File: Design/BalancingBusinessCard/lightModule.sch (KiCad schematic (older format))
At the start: 0 parts

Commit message: Made a part
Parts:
- added D? (x9): LED, symbol Device:LED
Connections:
- new net GND: D?.1 (K), D?.1 (K), D?.1 (K), D?.1 (K), D?.1 (K), D?.1 (K), D?.1 (K), D?.1 (K), D?.1 (K)
- new net LED_0: D?.2 (A)
- new net LED_1: D?.2 (A)
- new net LED_2: D?.2 (A)
- new net LED_3: D?.2 (A)
- new net LED_4: D?.2 (A)
- new net LED_5: D?.2 (A)
- new net LED_6: D?.2 (A)
- new net LED_7: D?.2 (A)
- new net LED_8: D?.2 (A)

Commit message: Assigned numbers
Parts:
- gave numbers to parts that had none: 9
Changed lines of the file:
@@
 $EndDescr
 $Comp
-L Device:LED D?
+L Device:LED D302
 U 1 1 5BCBC85A
 P 3900 2800
-F 0 "D?" V 3938 2683 50  0000 R CNN
+F 0 "D302" V 3938 2683 50  0000 R CNN
 F 1 "LED" V 3847 2683 50  0000 R CNN
 F 2 "" H 3900 2800 50  0001 C CNN
@@
 LED_1
 $Comp
-L power:GND #PWR?
+L power:GND #PWR0117
 U 1 1 5BCBC9E3
 P 3900 3050
-F 0 "#PWR?" H 3900 2800 50  0001 C CNN
+F 0 "#PWR0117" H 3900 2800 50  0001 C CNN
 F 1 "GND" H 3905 2877 50  0000 C CNN
 F 2 "" H 3900 3050 50  0001 C CNN
@@
 	3900 2950 3900 3050
 $Comp
-L Device:LED D?
+L Device:LED D303
 U 1 1 5BCBCA64
 P 4250 2800
-F 0 "D?" V 4288 2683 50  0000 R CNN
+F 0 "D303" V 4288 2683 50  0000 R CNN
 F 1 "LED" V 4197 2683 50  0000 R CNN
 F 2 "" H 4250 2800 50  0001 C CNN
@@
 LED_2
 $Comp
-L power:GND #PWR?
+L power:GND #PWR0118
 U 1 1 5BCBCA6C
 P 4250 3050
-F 0 "#PWR?" H 4250 2800 50  0001 C CNN
+F 0 "#PWR0118" H 4250 2800 50  0001 C CNN
 F 1 "GND" H 4255 2877 50  0000 C CNN
 F 2 "" H 4250 3050 50  0001 C CNN
@@
 	4250 2950 4250 3050
 $Comp
-L Device:LED D?
+L Device:LED D304
 U 1 1 5BCBCA94
 P 4600 2800
-F 0 "D?" V 4638 2683 50  0000 R CNN
+F 0 "D304" V 4638 2683 50  0000 R CNN
 F 1 "LED" V 4547 2683 50  0000 R CNN
 F 2 "" H 4600 2800 50  0001 C CNN
@@
 LED_3
 $Comp
-L power:GND #PWR?
+L power:GND #PWR0119
 U 1 1 5BCBCA9C
 P 4600 3050
-F 0 "#PWR?" H 4600 2800 50  0001 C CNN
+F 0 "#PWR0119" H 4600 2800 50  0001 C CNN
 F 1 "GND" H 4605 2877 50  0000 C CNN
 F 2 "" H 4600 3050 50  0001 C CNN
@@
 	4600 2950 4600 3050
 $Comp
-L Device:LED D?
+L Device:LED D305
 U 1 1 5BCBCAE0
 P 4950 2800
-F 0 "D?" V 4988 2683 50  0000 R CNN
+F 0 "D305" V 4988 2683 50  0000 R CNN
 F 1 "LED" V 4897 2683 50  0000 R CNN
 F 2 "" H 4950 2800 50  0001 C CNN
@@
 LED_4
 $Comp
-L power:GND #PWR?
+L power:GND #PWR0120
 U 1 1 5BCBCAE8
 P 4950 3050
-F 0 "#PWR?" H 4950 2800 50  0001 C CNN
+F 0 "#PWR0120" H 4950 2800 50  0001 C CNN
 F 1 "GND" H 4955 2877 50  0000 C CNN
 F 2 "" H 4950 3050 50  0001 C CNN
@@
 	4950 2950 4950 3050
 $Comp
-L Device:LED D?
+L Device:LED D306
 U 1 1 5BCBCB54
 P 5300 2800
-F 0 "D?" V 5338 2683 50  0000 R CNN
+F 0 "D306" V 5338 2683 50  0000 R CNN
 F 1 "LED" V 5247 2683 50  0000 R CNN
 F 2 "" H 5300 2800 50  0001 C CNN
@@
 LED_5
 $Comp
-L power:GND #PWR?
+L power:GND #PWR0121
 U 1 1 5BCBCB5C
 P 5300 3050
-F 0 "#PWR?" H 5300 2800 50  0001 C CNN
+F 0 "#PWR0121" H 5300 2800 50  0001 C CNN
 F 1 "GND" H 5305 2877 50  0000 C CNN
 F 2 "" H 5300 3050 50  0001 C CNN
@@
 	5300 2950 5300 3050
 $Comp
-L Device:LED D?
+L Device:LED D307
 U 1 1 5BCBCC00
 P 5650 2800
-F 0 "D?" V 5688 2683 50  0000 R CNN
+F 0 "D307" V 5688 2683 50  0000 R CNN
 F 1 "LED" V 5597 2683 50  0000 R CNN
 F 2 "" H 5650 2800 50  0001 C CNN
@@
 LED_6
 $Comp
-L power:GND #PWR?
+L power:GND #PWR0122
 U 1 1 5BCBCC08
 P 5650 3050
-F 0 "#PWR?" H 5650 2800 50  0001 C CNN
+F 0 "#PWR0122" H 5650 2800 50  0001 C CNN
 F 1 "GND" H 5655 2877 50  0000 C CNN
 F 2 "" H 5650 3050 50  0001 C CNN
@@
 	5650 2950 5650 3050
 $Comp
-L Device:LED D?
+L Device:LED D308
 U 1 1 5BCBCCF0
 P 6000 2800
-F 0 "D?" V 6038 2683 50  0000 R CNN
+F 0 "D308" V 6038 2683 50  0000 R CNN
 F 1 "LED" V 5947 2683 50  0000 R CNN
 F 2 "" H 6000 2800 50  0001 C CNN
@@
 LED_7
 $Comp
-L power:GND #PWR?
+L power:GND #PWR0123
 U 1 1 5BCBCCF8
 P 6000 3050
-F 0 "#PWR?" H 6000 2800 50  0001 C CNN
+F 0 "#PWR0123" H 6000 2800 50  0001 C CNN
 F 1 "GND" H 6005 2877 50  0000 C CNN
 F 2 "" H 6000 3050 50  0001 C CNN
@@
 	6000 2950 6000 3050
 $Comp
-L Device:LED D?
+L Device:LED D301
 U 1 1 5BCBD2AC
 P 3550 2800
-F 0 "D?" V 3588 2683 50  0000 R CNN
+F 0 "D301" V 3588 2683 50  0000 R CNN
 F 1 "LED" V 3497 2683 50  0000 R CNN
 F 2 "" H 3550 2800 50  0001 C CNN
@@
 LED_0
 $Comp
-L power:GND #PWR?
+L power:GND #PWR0124
 U 1 1 5BCBD2B4
 P 3550 3050
-F 0 "#PWR?" H 3550 2800 50  0001 C CNN
+F 0 "#PWR0124" H 3550 2800 50  0001 C CNN
 F 1 "GND" H 3555 2877 50  0000 C CNN
 F 2 "" H 3550 3050 50  0001 C CNN
@@
 	3550 2950 3550 3050
 $Comp
-L Device:LED D?
+L Device:LED D309
 U 1 1 5BCBD4AC
 P 6350 2800
-F 0 "D?" V 6388 2683 50  0000 R CNN
+F 0 "D309" V 6388 2683 50  0000 R CNN
 F 1 "LED" V 6297 2683 50  0000 R CNN
 F 2 "" H 6350 2800 50  0001 C CNN
@@
 LED_8
 $Comp
-L power:GND #PWR?
+L power:GND #PWR0125
 U 1 1 5BCBD4B4
 P 6350 3050
-F 0 "#PWR?" H 6350 2800 50  0001 C CNN
+F 0 "#PWR0125" H 6350 2800 50  0001 C CNN
 F 1 "GND" H 6355 2877 50  0000 C CNN
 F 2 "" H 6350 3050 50  0001 C CNN

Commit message: Footprint assignment
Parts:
- D301, D302, D303, D304, D305, D306, D307, D308, D309: footprint (none) -> LED_SMD:LED_0603_1608Metric
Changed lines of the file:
@@
 F 0 "D302" V 3938 2683 50  0000 R CNN
 F 1 "LED" V 3847 2683 50  0000 R CNN
-F 2 "" H 3900 2800 50  0001 C CNN
+F 2 "LED_SMD:LED_0603_1608Metric" H 3900 2800 50  0001 C CNN
 F 3 "~" H 3900 2800 50  0001 C CNN
 	1    3900 2800
@@
 F 0 "D303" V 4288 2683 50  0000 R CNN
 F 1 "LED" V 4197 2683 50  0000 R CNN
-F 2 "" H 4250 2800 50  0001 C CNN
+F 2 "LED_SMD:LED_0603_1608Metric" H 4250 2800 50  0001 C CNN
 F 3 "~" H 4250 2800 50  0001 C CNN
 	1    4250 2800
@@
 F 0 "D304" V 4638 2683 50  0000 R CNN
 F 1 "LED" V 4547 2683 50  0000 R CNN
-F 2 "" H 4600 2800 50  0001 C CNN
+F 2 "LED_SMD:LED_0603_1608Metric" H 4600 2800 50  0001 C CNN
 F 3 "~" H 4600 2800 50  0001 C CNN
 	1    4600 2800
@@
 F 0 "D305" V 4988 2683 50  0000 R CNN
 F 1 "LED" V 4897 2683 50  0000 R CNN
-F 2 "" H 4950 2800 50  0001 C CNN
+F 2 "LED_SMD:LED_0603_1608Metric" H 4950 2800 50  0001 C CNN
 F 3 "~" H 4950 2800 50  0001 C CNN
 	1    4950 2800
@@
 F 0 "D306" V 5338 2683 50  0000 R CNN
 F 1 "LED" V 5247 2683 50  0000 R CNN
-F 2 "" H 5300 2800 50  0001 C CNN
+F 2 "LED_SMD:LED_0603_1608Metric" H 5300 2800 50  0001 C CNN
 F 3 "~" H 5300 2800 50  0001 C CNN
 	1    5300 2800
@@
 F 0 "D307" V 5688 2683 50  0000 R CNN
 F 1 "LED" V 5597 2683 50  0000 R CNN
-F 2 "" H 5650 2800 50  0001 C CNN
+F 2 "LED_SMD:LED_0603_1608Metric" H 5650 2800 50  0001 C CNN
 F 3 "~" H 5650 2800 50  0001 C CNN
 	1    5650 2800
@@
 F 0 "D308" V 6038 2683 50  0000 R CNN
 F 1 "LED" V 5947 2683 50  0000 R CNN
-F 2 "" H 6000 2800 50  0001 C CNN
+F 2 "LED_SMD:LED_0603_1608Metric" H 6000 2800 50  0001 C CNN
 F 3 "~" H 6000 2800 50  0001 C CNN
 	1    6000 2800
@@
 F 0 "D301" V 3588 2683 50  0000 R CNN
 F 1 "LED" V 3497 2683 50  0000 R CNN
-F 2 "" H 3550 2800 50  0001 C CNN
+F 2 "LED_SMD:LED_0603_1608Metric" H 3550 2800 50  0001 C CNN
 F 3 "~" H 3550 2800 50  0001 C CNN
 	1    3550 2800
@@
 F 0 "D309" V 6388 2683 50  0000 R CNN
 F 1 "LED" V 6297 2683 50  0000 R CNN
-F 2 "" H 6350 2800 50  0001 C CNN
+F 2 "LED_SMD:LED_0603_1608Metric" H 6350 2800 50  0001 C CNN
 F 3 "~" H 6350 2800 50  0001 C CNN
 	1    6350 2800

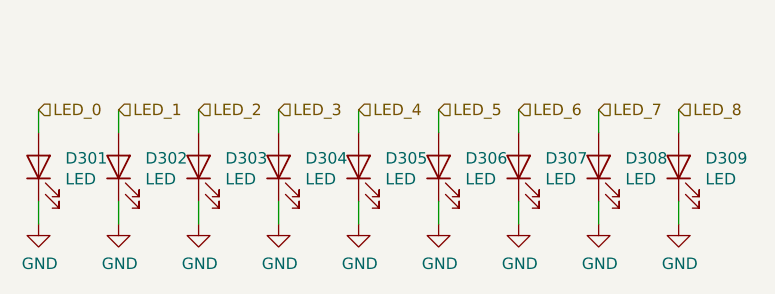
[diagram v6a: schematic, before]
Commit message: Completed Lights board schematic
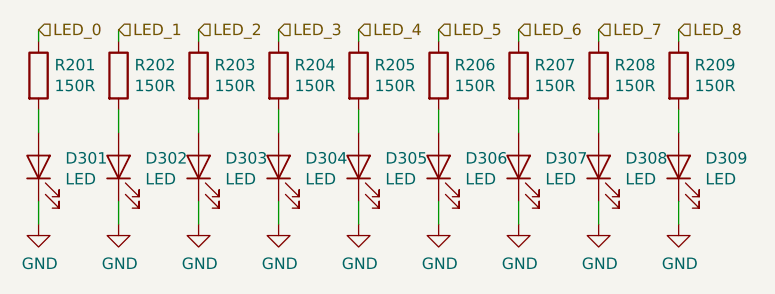
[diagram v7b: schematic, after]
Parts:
- added R201, R202, R203, R204, R205, R206, R207, R208, R209: 150R, Resistors_SMD:R_0603, symbol Device:R
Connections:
- net LED_0: now also R201.1; no longer D301.2 (A)
- net LED_1: now also R202.1; no longer D302.2 (A)
- net LED_2: now also R203.1; no longer D303.2 (A)
- net LED_3: now also R204.1; no longer D304.2 (A)
- net LED_4: now also R205.1; no longer D305.2 (A)
- net LED_5: now also R206.1; no longer D306.2 (A)
- net LED_6: now also R207.1; no longer D307.2 (A)
- net LED_7: now also R208.1; no longer D308.2 (A)
- net LED_8: now also R209.1; no longer D309.2 (A)
- new net: D302.2 (A), R202.2
- new net: D303.2 (A), R203.2
- new net: D304.2 (A), R204.2
- new net: D305.2 (A), R205.2
- new net: D306.2 (A), R206.2
- new net: D307.2 (A), R207.2
- new net: D308.2 (A), R208.2
- new net: D301.2 (A), R201.2
- new net: D309.2 (A), R209.2
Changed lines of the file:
@@
 EESchema Schematic File Version 4
-LIBS:BalancingBusinessCard-cache
+LIBS:BalancingBusinessCardLights-cache
 EELAYER 26 0
 EELAYER END
 $Descr A4 11693 8268
 encoding utf-8
-Sheet 3 5
+Sheet 2 4
 Title ""
 Date ""
@@
 	0    -1   -1   0
 $EndComp
-Text HLabel 3900 2550 2    50   Input ~ 0
+Text HLabel 3900 2200 2    50   Input ~ 0
 LED_1
 $Comp
@@
 	0    -1   -1   0
 $EndComp
-Text HLabel 4250 2550 2    50   Input ~ 0
+Text HLabel 4250 2200 2    50   Input ~ 0
 LED_2
 $Comp
@@
 	0    -1   -1   0
 $EndComp
-Text HLabel 4600 2550 2    50   Input ~ 0
+Text HLabel 4600 2200 2    50   Input ~ 0
 LED_3
 $Comp
@@
 	0    -1   -1   0
 $EndComp
-Text HLabel 4950 2550 2    50   Input ~ 0
+Text HLabel 4950 2200 2    50   Input ~ 0
 LED_4
 $Comp
@@
 	0    -1   -1   0
 $EndComp
-Text HLabel 5300 2550 2    50   Input ~ 0
+Text HLabel 5300 2200 2    50   Input ~ 0
 LED_5
 $Comp
@@
 	0    -1   -1   0
 $EndComp
-Text HLabel 5650 2550 2    50   Input ~ 0
+Text HLabel 5650 2200 2    50   Input ~ 0
 LED_6
 $Comp
@@
 	0    -1   -1   0
 $EndComp
-Text HLabel 6000 2550 2    50   Input ~ 0
+Text HLabel 6000 2200 2    50   Input ~ 0
 LED_7
 $Comp
@@
 	0    -1   -1   0
 $EndComp
-Text HLabel 3550 2550 2    50   Input ~ 0
+Text HLabel 3550 2200 2    50   Input ~ 0
 LED_0
 $Comp
@@
 	0    -1   -1   0
 $EndComp
-Text HLabel 6350 2550 2    50   Input ~ 0
+Text HLabel 6350 2200 2    50   Input ~ 0
 LED_8
 $Comp
@@
 Wire Wire Line
 	6350 2950 6350 3050
+$Comp
+L Device:R R201
+U 1 1 5C0EA341
+P 3550 2400
+F 0 "R201" H 3620 2446 50  0000 L CNN
+F 1 "150R" H 3620 2355 50  0000 L CNN
+F 2 "Resistors_SMD:R_0603" V 3480 2400 50  0001 C CNN
+F 3 "~" H 3550 2400 50  0001 C CNN
+	1    3550 2400
+	1    0    0    -1
+$EndComp
+Wire Wire Line
+	3550 2250 3550 2200
+$Comp
+L Device:R R202
+U 1 1 5C0EA8FF
+P 3900 2400
+F 0 "R202" H 3970 2446 50  0000 L CNN
+F 1 "150R" H 3970 2355 50  0000 L CNN
+F 2 "Resistors_SMD:R_0603" V 3830 2400 50  0001 C CNN
+F 3 "~" H 3900 2400 50  0001 C CNN
+	1    3900 2400
+	1    0    0    -1
+$EndComp
+$Comp
+L Device:R R203
+U 1 1 5C0EA93D
+P 4250 2400
+F 0 "R203" H 4320 2446 50  0000 L CNN
+F 1 "150R" H 4320 2355 50  0000 L CNN
+F 2 "Resistors_SMD:R_0603" V 4180 2400 50  0001 C CNN
+F 3 "~" H 4250 2400 50  0001 C CNN
+	1    4250 2400
+	1    0    0    -1
+$EndComp
+$Comp
+L Device:R R204
+U 1 1 5C0EA97D
+P 4600 2400
+F 0 "R204" H 4670 2446 50  0000 L CNN
+F 1 "150R" H 4670 2355 50  0000 L CNN
+F 2 "Resistors_SMD:R_0603" V 4530 2400 50  0001 C CNN
+F 3 "~" H 4600 2400 50  0001 C CNN
+	1    4600 2400
+	1    0    0    -1
+$EndComp
+$Comp
+L Device:R R205
+U 1 1 5C0EA9B5
+P 4950 2400
+F 0 "R205" H 5020 2446 50  0000 L CNN
+F 1 "150R" H 5020 2355 50  0000 L CNN
+F 2 "Resistors_SMD:R_0603" V 4880 2400 50  0001 C CNN
+F 3 "~" H 4950 2400 50  0001 C CNN
+	1    4950 2400
+	1    0    0    -1
+$EndComp
+$Comp
+L Device:R R206
+U 1 1 5C0EA9FD
+P 5300 2400
+F 0 "R206" H 5370 2446 50  0000 L CNN
+F 1 "150R" H 5370 2355 50  0000 L CNN
+F 2 "Resistors_SMD:R_0603" V 5230 2400 50  0001 C CNN
+F 3 "~" H 5300 2400 50  0001 C CNN
+	1    5300 2400
+	1    0    0    -1
+$EndComp
+$Comp
+L Device:R R207
+U 1 1 5C0EAA3F
+P 5650 2400
+F 0 "R207" H 5720 2446 50  0000 L CNN
+F 1 "150R" H 5720 2355 50  0000 L CNN
+F 2 "Resistors_SMD:R_0603" V 5580 2400 50  0001 C CNN
+F 3 "~" H 5650 2400 50  0001 C CNN
+	1    5650 2400
+	1    0    0    -1
+$EndComp
+$Comp
+L Device:R R208
+U 1 1 5C0EAA7D
+P 6000 2400
+F 0 "R208" H 6070 2446 50  0000 L CNN
+F 1 "150R" H 6070 2355 50  0000 L CNN
+F 2 "Resistors_SMD:R_0603" V 5930 2400 50  0001 C CNN
+F 3 "~" H 6000 2400 50  0001 C CNN
+	1    6000 2400
+	1    0    0    -1
+$EndComp
+$Comp
+L Device:R R209
+U 1 1 5C0EAAC7
+P 6350 2400
+F 0 "R209" H 6420 2446 50  0000 L CNN
+F 1 "150R" H 6420 2355 50  0000 L CNN
+F 2 "Resistors_SMD:R_0603" V 6280 2400 50  0001 C CNN
+F 3 "~" H 6350 2400 50  0001 C CNN
+	1    6350 2400
+	1    0    0    -1
+$EndComp
+Wire Wire Line
+	3900 2250 3900 2200
+Wire Wire Line
+	4250 2250 4250 2200
+Wire Wire Line
+	4600 2250 4600 2200
+Wire Wire Line
+	4950 2250 4950 2200
+Wire Wire Line
+	5300 2250 5300 2200
+Wire Wire Line
+	5650 2250 5650 2200
+Wire Wire Line
+	6000 2250 6000 2200
+Wire Wire Line
+	6350 2250 6350 2200
 $EndSCHEMATC

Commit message: Began v3 board design
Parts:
- R201, R202, R203, R204, R205, R206, R207, R208, R209: footprint Resistors_SMD:R_0603 -> Resistor_SMD:R_0603_1608Metric
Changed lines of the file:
@@
 EESchema Schematic File Version 4
-LIBS:BalancingBusinessCardLights-cache
 EELAYER 26 0
 EELAYER END
@@
 F 0 "R201" H 3620 2446 50  0000 L CNN
 F 1 "150R" H 3620 2355 50  0000 L CNN
-F 2 "Resistors_SMD:R_0603" V 3480 2400 50  0001 C CNN
+F 2 "Resistor_SMD:R_0603_1608Metric" V 3480 2400 50  0001 C CNN
 F 3 "~" H 3550 2400 50  0001 C CNN
 	1    3550 2400
@@
 F 0 "R202" H 3970 2446 50  0000 L CNN
 F 1 "150R" H 3970 2355 50  0000 L CNN
-F 2 "Resistors_SMD:R_0603" V 3830 2400 50  0001 C CNN
+F 2 "Resistor_SMD:R_0603_1608Metric" V 3830 2400 50  0001 C CNN
 F 3 "~" H 3900 2400 50  0001 C CNN
 	1    3900 2400
@@
 F 0 "R203" H 4320 2446 50  0000 L CNN
 F 1 "150R" H 4320 2355 50  0000 L CNN
-F 2 "Resistors_SMD:R_0603" V 4180 2400 50  0001 C CNN
+F 2 "Resistor_SMD:R_0603_1608Metric" V 4180 2400 50  0001 C CNN
 F 3 "~" H 4250 2400 50  0001 C CNN
 	1    4250 2400
@@
 F 0 "R204" H 4670 2446 50  0000 L CNN
 F 1 "150R" H 4670 2355 50  0000 L CNN
-F 2 "Resistors_SMD:R_0603" V 4530 2400 50  0001 C CNN
+F 2 "Resistor_SMD:R_0603_1608Metric" V 4530 2400 50  0001 C CNN
 F 3 "~" H 4600 2400 50  0001 C CNN
 	1    4600 2400
@@
 F 0 "R205" H 5020 2446 50  0000 L CNN
 F 1 "150R" H 5020 2355 50  0000 L CNN
-F 2 "Resistors_SMD:R_0603" V 4880 2400 50  0001 C CNN
+F 2 "Resistor_SMD:R_0603_1608Metric" V 4880 2400 50  0001 C CNN
 F 3 "~" H 4950 2400 50  0001 C CNN
 	1    4950 2400
@@
 F 0 "R206" H 5370 2446 50  0000 L CNN
 F 1 "150R" H 5370 2355 50  0000 L CNN
-F 2 "Resistors_SMD:R_0603" V 5230 2400 50  0001 C CNN
+F 2 "Resistor_SMD:R_0603_1608Metric" V 5230 2400 50  0001 C CNN
 F 3 "~" H 5300 2400 50  0001 C CNN
 	1    5300 2400
@@
 F 0 "R207" H 5720 2446 50  0000 L CNN
 F 1 "150R" H 5720 2355 50  0000 L CNN
-F 2 "Resistors_SMD:R_0603" V 5580 2400 50  0001 C CNN
+F 2 "Resistor_SMD:R_0603_1608Metric" V 5580 2400 50  0001 C CNN
 F 3 "~" H 5650 2400 50  0001 C CNN
 	1    5650 2400
@@
 F 0 "R208" H 6070 2446 50  0000 L CNN
 F 1 "150R" H 6070 2355 50  0000 L CNN
-F 2 "Resistors_SMD:R_0603" V 5930 2400 50  0001 C CNN
+F 2 "Resistor_SMD:R_0603_1608Metric" V 5930 2400 50  0001 C CNN
 F 3 "~" H 6000 2400 50  0001 C CNN
 	1    6000 2400
@@
 F 0 "R209" H 6420 2446 50  0000 L CNN
 F 1 "150R" H 6420 2355 50  0000 L CNN
-F 2 "Resistors_SMD:R_0603" V 6280 2400 50  0001 C CNN
+F 2 "Resistor_SMD:R_0603_1608Metric" V 6280 2400 50  0001 C CNN
 F 3 "~" H 6350 2400 50  0001 C CNN
 	1    6350 2400
